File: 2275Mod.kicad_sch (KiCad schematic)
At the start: 22 parts, among them IC1 LTV-356T, J1 640388-8, K1 40.52.8.024.5000, K2 G5LE-14-CF_DC24, U1 LM340LAZ-5.0, U2 TCLT1600, U3 TCLT1600, q1 NPN_Transistor

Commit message: commit before starting kicad 7
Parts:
- C1: footprint (none) -> Capacitor_THT:C_Rect_L10.0mm_W4.0mm_P7.50mm_MKS4
- C2: footprint (none) -> Capacitor_THT:CP_Radial_D16.0mm_P7.50mm
- C3: footprint (none) -> Capacitor_THT:CP_Radial_D5.0mm_P2.50mm
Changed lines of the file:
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@@
       (effects (font (size 1.27 1.27)) (justify left))
     )
-    (property "Footprint" "" (id 2) (at 254.9652 97.79 0)
+    (property "Footprint" "Capacitor_THT:CP_Radial_D5.0mm_P2.50mm" (id 2) (at 254.9652 97.79 0)
       (effects (font (size 1.27 1.27)) hide)
     )
@@
       (effects (font (size 1.27 1.27)) (justify left))
     )
-    (property "Footprint" "" (id 2) (at 77.47 95.25 0)
+    (property "Footprint" "Capacitor_THT:C_Rect_L10.0mm_W4.0mm_P7.50mm_MKS4" (id 2) (at 77.47 95.25 0)
       (effects (font (size 1.27 1.27)) hide)
     )
@@
       (effects (font (size 1.27 1.27)) (justify left))
     )
-    (property "Footprint" "" (id 2) (at 215.5952 96.52 0)
+    (property "Footprint" "Capacitor_THT:CP_Radial_D16.0mm_P7.50mm" (id 2) (at 215.5952 96.52 0)
       (effects (font (size 1.27 1.27)) hide)
     )
@@
     )
     (path "/af6d24d3-2ebe-4f80-9d0c-f289817d2611"
-      (reference "C1") (unit 1) (value ".01/400v") (footprint "")
+      (reference "C1") (unit 1) (value ".01/400v") (footprint "Capacitor_THT:C_Rect_L10.0mm_W4.0mm_P7.50mm_MKS4")
     )
     (path "/f943cf73-6023-4201-8914-d783c8da9ec4"
-      (reference "C2") (unit 1) (value "1000uf") (footprint "")
+      (reference "C2") (unit 1) (value "1000uf") (footprint "Capacitor_THT:CP_Radial_D16.0mm_P7.50mm")
     )
     (path "/281740b4-9504-4250-8402-6cda37c9fff4"
-      (reference "C3") (unit 1) (value "10uf") (footprint "")
+      (reference "C3") (unit 1) (value "10uf") (footprint "Capacitor_THT:CP_Radial_D5.0mm_P2.50mm")
     )
     (path "/9ee275cc-47c1-4b8b-980c-7d7214ee4bde/5b26e194-09b4-48bf-9fc7-24c57264e72b"
@@
     )
     (path "/9ee275cc-47c1-4b8b-980c-7d7214ee4bde/b240069a-d2aa-48dc-9bba-60a372f4e603"
-      (reference "C201") (unit 1) (value "4700uf") (footprint "")
+      (reference "C201") (unit 1) (value "4700uf") (footprint "Capacitor_THT:CP_Radial_D25.0mm_P10.00mm_SnapIn")
     )
     (path "/1c064150-4a5c-4345-8f52-f032fa5cdc84"
@@
     )
     (path "/9ee275cc-47c1-4b8b-980c-7d7214ee4bde/4f791885-332d-4c42-9ab4-d18f400bce56"
-      (reference "R205") (unit 1) (value "220") (footprint "")
+      (reference "R205") (unit 1) (value "220") (footprint "Resistor_SMD:R_0805_2012Metric_Pad1.20x1.40mm_HandSolder")
     )
     (path "/44cf2d32-8e8c-4f2d-a00f-594cc953fa48"

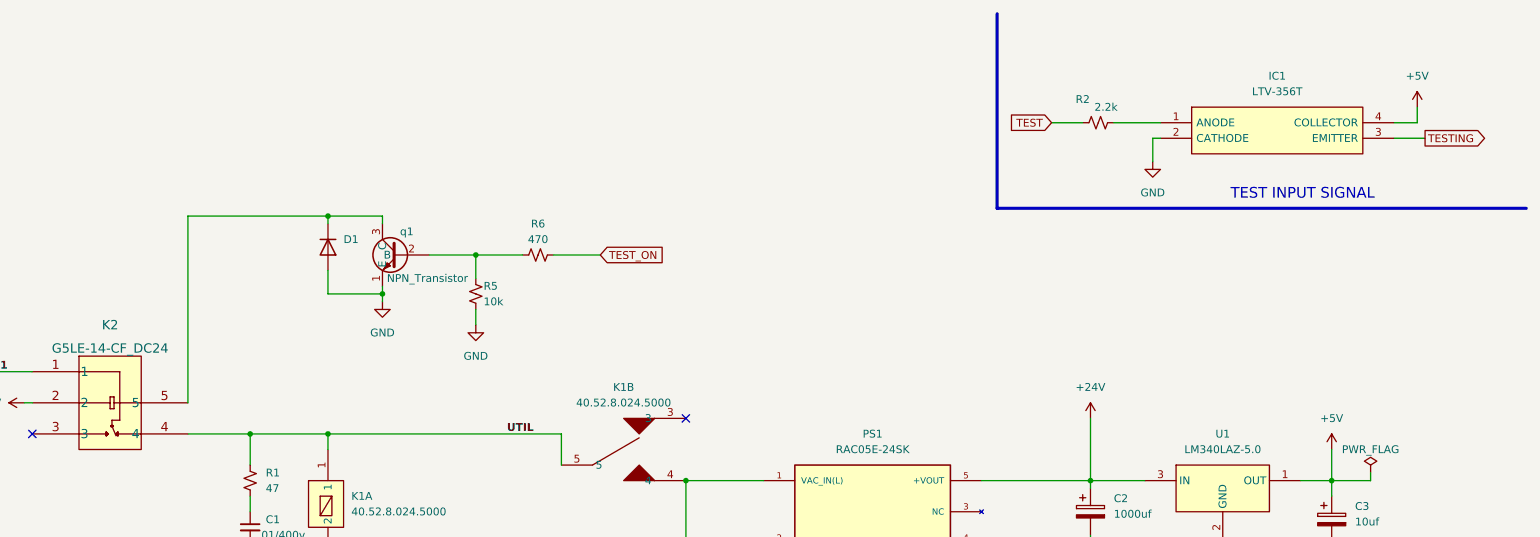
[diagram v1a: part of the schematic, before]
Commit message: move parts on the PCB
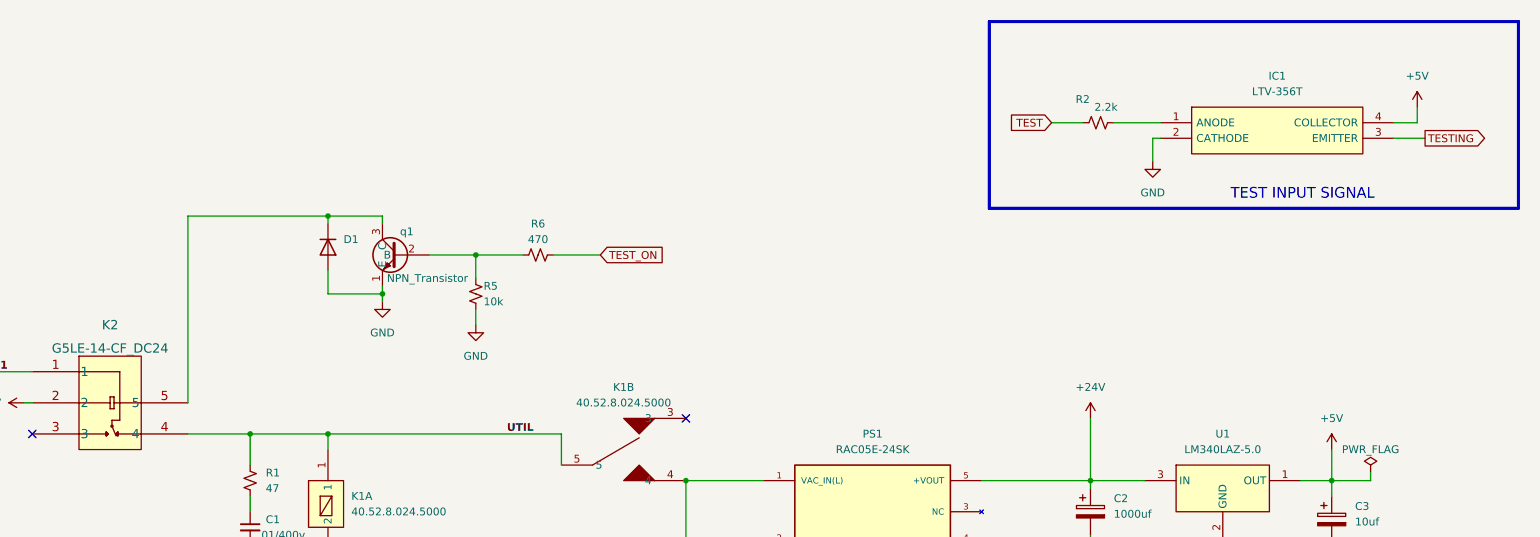
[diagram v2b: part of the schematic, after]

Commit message: add test points, clean up errors
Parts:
- added TP1, TP2, TP3: 5019, AAA_Misc:KEYSTONE_5019, symbol AAA_Misc:5019
- C1: footprint Capacitor_THT:C_Rect_L10.0mm_W4.0mm_P7.50mm_MKS4 -> AAA_Misc:KEYSTONE_5019
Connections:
- net +24V: now also TP1.TP
- net +5V: now also TP2.TP
- net GND: now also TP3.TP
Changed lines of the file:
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@@
   (junction (at 254 87.63) (diameter 0) (color 0 0 0 0)
   )
+  (junction (at 203.2 97.79) (diameter 0) (color 0 0 0 0)
+  )
+  (junction (at 254 78.74) (diameter 0) (color 0 0 0 0)
+  )
   (junction (at 77.47 102.87) (diameter 0) (color 0 0 0 0)
   )
@@
   )
   (junction (at 214.63 97.79) (diameter 0) (color 0 0 0 0)
+  )
+  (junction (at 214.63 80.01) (diameter 0) (color 0 0 0 0)
   )
   (junction (at 77.47 80.01) (diameter 0) (color 0 0 0 0)
@@
     (stroke (width 0) (type default))
   )
+  (wire (pts (xy 214.63 80.01) (xy 214.63 87.63))
+    (stroke (width 0) (type default))
+  )
+  (wire (pts (xy 254 78.74) (xy 256.54 78.74))
+    (stroke (width 0) (type default))
+  )
   (polyline (pts (xy 20.32 166.37) (xy 20.32 196.85))
     (stroke (width 0.5) (type solid) (color 0 0 0 1))
   )
+  (wire (pts (xy 254 78.74) (xy 254 77.47))
+    (stroke (width 0) (type default))
+  )
   (polyline (pts (xy 92.71 166.37) (xy 20.32 166.37))
     (stroke (width 0.5) (type solid) (color 0 0 0 1))
   )
+  (wire (pts (xy 212.09 80.01) (xy 214.63 80.01))
+    (stroke (width 0) (type default))
+  )
   (wire (pts (xy 248.92 87.63) (xy 254 87.63))
     (stroke (width 0) (type default))
@@
     (stroke (width 0) (type default))
   )
-  (wire (pts (xy 254 87.63) (xy 254 82.55))
+  (wire (pts (xy 254 87.63) (xy 254 78.74))
     (stroke (width 0) (type default))
   )
@@
     (stroke (width 0.5) (type solid) (color 0 0 0 1))
   )
+  (wire (pts (xy 203.2 97.79) (xy 214.63 97.79))
+    (stroke (width 0) (type default))
+  )
   (wire (pts (xy 226.06 31.75) (xy 224.79 31.75))
     (stroke (width 0) (type default))
@@
     (stroke (width 0) (type default))
   )
-  (wire (pts (xy 196.85 97.79) (xy 214.63 97.79))
+  (wire (pts (xy 196.85 97.79) (xy 203.2 97.79))
     (stroke (width 0) (type default))
   )
@@
     (stroke (width 0) (type default))
   )
+  (wire (pts (xy 203.2 97.79) (xy 203.2 100.33))
+    (stroke (width 0) (type default))
+  )
   (wire (pts (xy 77.47 102.87) (xy 90.17 102.87))
     (stroke (width 0) (type default))
@@
     (stroke (width 0) (type default))
   )
+  (wire (pts (xy 254 132.08) (xy 260.35 132.08))
+    (stroke (width 0) (type default))
+  )
   (wire (pts (xy 127 50.8) (xy 134.62 50.8))
     (stroke (width 0) (type default))
@@
     (stroke (width 0) (type default))
   )
-  (wire (pts (xy 214.63 77.47) (xy 214.63 87.63))
+  (wire (pts (xy 214.63 77.47) (xy 214.63 80.01))
     (stroke (width 0) (type default))
   )
@@
   (label "G_L1" (at 101.6 176.53 0) (fields_autoplaced)
     (effects (font (size 1.27 1.27) bold) (justify left bottom))
+  )
+  (label "+24V" (at 204.47 87.63 0) (fields_autoplaced)
+    (effects (font (size 1.27 1.27)) (justify left bottom))
+  )
+  (label "5VDC" (at 255.27 87.63 0) (fields_autoplaced)
+    (effects (font (size 1 1)) (justify left bottom))
   )
   (label "L1" (at 35.56 69.85 0) (fields_autoplaced)
@@
         (path "/6ee24427-09ce-46d0-a3a3-2e623f3a3aa5"
           (reference "R5") (unit 1)
+        )
+      )
+    )
+  )
+  (symbol (lib_id "AAA_Misc:5019") (at 207.01 80.01 180) (unit 1)
+    (in_bom yes) (on_board yes) (dnp no) (fields_autoplaced)
+    (property "Reference" "TP1" (at 207.01 74.93 0)
+      (effects (font (size 1.27 1.27)))
+    )
+    (property "Value" "5019" (at 207.01 77.47 0)
+      (effects (font (size 1.27 1.27)))
+    )
+    (property "Footprint" "AAA_Misc:KEYSTONE_5019" (at 203.2 76.2 0)
+      (effects (font (size 1.27 1.27)) (justify left bottom) hide)
+    )
+    (property "Datasheet" "" (at 207.01 80.01 0)
+      (effects (font (size 1.27 1.27)) (justify left bottom) hide)
+    )
+    (property "PARTREV" "D" (at 207.01 80.01 0)
+      (effects (font (size 1.27 1.27)) (justify left bottom) hide)
+    )
+    (property "STANDARD" "Manufacturer Recommendations" (at 205.74 82.55 0)
+      (effects (font (size 1.27 1.27)) (justify left bottom) hide)
+    )
+    (property "MAXIMUM_PACKAGE_HEIGHT" "2.29 mm" (at 201.93 80.01 0)
+      (effects (font (size 1.27 1.27)) (justify left bottom) hide)
+    )
+    (property "MANUFACTURER" "Keystone Electronics" (at 205.74 83.82 0)
+      (effects (font (size 1.27 1.27)) (justify left bottom) hide)
+    )
+    (property "SNAPEDA_PN" "5019" (at 214.63 74.93 0)
+      (effects (font (size 1.27 1.27)) (justify left bottom) hide)
+    )
+    (pin "TP")
+    (instances
+      (project "2275Mod"
+        (path "/6ee24427-09ce-46d0-a3a3-2e623f3a3aa5"
+          (reference "TP1") (unit 1)
         )
       )
@@
     )
   )
+  (symbol (lib_id "AAA_Misc:5019") (at 261.62 78.74 0) (unit 1)
+    (in_bom yes) (on_board yes) (dnp no) (fields_autoplaced)
+    (property "Reference" "TP2" (at 264.16 78.105 0)
+      (effects (font (size 1.27 1.27)) (justify left))
+    )
+    (property "Value" "5019" (at 264.16 80.645 0)
+      (effects (font (size 1.27 1.27)) (justify left))
+    )
+    (property "Footprint" "AAA_Misc:KEYSTONE_5019" (at 265.43 82.55 0)
+      (effects (font (size 1.27 1.27)) (justify left bottom) hide)
+    )
+    (property "Datasheet" "" (at 261.62 78.74 0)
+      (effects (font (size 1.27 1.27)) (justify left bottom) hide)
+    )
+    (property "PARTREV" "D" (at 261.62 78.74 0)
+      (effects (font (size 1.27 1.27)) (justify left bottom) hide)
+    )
+    (property "STANDARD" "Manufacturer Recommendations" (at 262.89 76.2 0)
+      (effects (font (size 1.27 1.27)) (justify left bottom) hide)
+    )
+    (property "MAXIMUM_PACKAGE_HEIGHT" "2.29 mm" (at 266.7 78.74 0)
+      (effects (font (size 1.27 1.27)) (justify left bottom) hide)
+    )
+    (property "MANUFACTURER" "Keystone Electronics" (at 262.89 74.93 0)
+      (effects (font (size 1.27 1.27)) (justify left bottom) hide)
+    )
+    (property "SNAPEDA_PN" "5019" (at 254 83.82 0)
+      (effects (font (size 1.27 1.27)) (justify left bottom) hide)
+    )
+    (pin "TP")
+    (instances
+      (project "2275Mod"
+        (path "/6ee24427-09ce-46d0-a3a3-2e623f3a3aa5"
+          (reference "TP2") (unit 1)
+        )
+      )
+    )
+  )
   (symbol (lib_id "Device:R_Small_US") (at 215.9 29.21 90) (unit 1)
     (in_bom yes) (on_board yes) (dnp no)
@@
     )
   )
+  (symbol (lib_id "AAA_Misc:5019") (at 203.2 105.41 270) (unit 1)
+    (in_bom yes) (on_board yes) (dnp no) (fields_autoplaced)
+    (property "Reference" "TP3" (at 205.74 104.775 90)
+      (effects (font (size 1.27 1.27)) (justify left))
+    )
+    (property "Value" "5019" (at 205.74 107.315 90)
+      (effects (font (size 1.27 1.27)) (justify left))
+    )
+    (property "Footprint" "AAA_Misc:KEYSTONE_5019" (at 199.39 109.22 0)
+      (effects (font (size 1.27 1.27)) (justify left bottom) hide)
+    )
+    (property "Datasheet" "" (at 203.2 105.41 0)
+      (effects (font (size 1.27 1.27)) (justify left bottom) hide)
+    )
+    (property "PARTREV" "D" (at 203.2 105.41 0)
+      (effects (font (size 1.27 1.27)) (justify left bottom) hide)
+    )
+    (property "STANDARD" "Manufacturer Recommendations" (at 205.74 106.68 0)
+      (effects (font (size 1.27 1.27)) (justify left bottom) hide)
+    )
+    (property "MAXIMUM_PACKAGE_HEIGHT" "2.29 mm" (at 203.2 110.49 0)
+      (effects (font (size 1.27 1.27)) (justify left bottom) hide)
+    )
+    (property "MANUFACTURER" "Keystone Electronics" (at 207.01 106.68 0)
+      (effects (font (size 1.27 1.27)) (justify left bottom) hide)
+    )
+    (property "SNAPEDA_PN" "5019" (at 198.12 97.79 0)
+      (effects (font (size 1.27 1.27)) (justify left bottom) hide)
+    )
+    (pin "TP")
+    (instances
+      (project "2275Mod"
+        (path "/6ee24427-09ce-46d0-a3a3-2e623f3a3aa5"
+          (reference "TP3") (unit 1)
+        )
+      )
+    )
+  )
   (symbol (lib_id "AAA_JH:LTV-356T") (at 226.06 29.21 0) (unit 1)
     (in_bom yes) (on_board yes) (dnp no) (fields_autoplaced)
@@
     )
   )
-  (symbol (lib_id "power:+5V") (at 254 82.55 0) (unit 1)
-    (in_bom yes) (on_board yes) (dnp no) (fields_autoplaced)
-    (property "Reference" "#PWR08" (at 254 86.36 0)
-      (effects (font (size 1.27 1.27)) hide)
-    )
-    (property "Value" "+5V" (at 254 77.47 0)
-      (effects (font (size 1.27 1.27)))
-    )
-    (property "Footprint" "" (at 254 82.55 0)
-      (effects (font (size 1.27 1.27)) hide)
-    )
-    (property "Datasheet" "" (at 254 82.55 0)
+  (symbol (lib_id "power:+5V") (at 254 77.47 0) (unit 1)
+    (in_bom yes) (on_board yes) (dnp no) (fields_autoplaced)
+    (property "Reference" "#PWR08" (at 254 81.28 0)
+      (effects (font (size 1.27 1.27)) hide)
+    )
+    (property "Value" "+5V" (at 254 72.39 0)
+      (effects (font (size 1.27 1.27)))
+    )
+    (property "Footprint" "" (at 254 77.47 0)
+      (effects (font (size 1.27 1.27)) hide)
+    )
+    (property "Datasheet" "" (at 254 77.47 0)
       (effects (font (size 1.27 1.27)) hide)
     )
@@
       (effects (font (size 1.27 1.27)) (justify left))
     )
-    (property "Footprint" "Capacitor_THT:C_Rect_L10.0mm_W4.0mm_P7.50mm_MKS4" (at 77.47 95.25 0)
+    (property "Footprint" "AAA_Misc:KEYSTONE_5019" (at 77.47 95.25 0)
       (effects (font (size 1.27 1.27)) hide)
     )
@@
       (effects (font (size 1.27 1.27)) hide)
     )
-    (property "Value" "PWR_FLAG" (at 260.35 82.55 0)
-      (effects (font (size 1.27 1.27)))
-    )
+    (property "Value" "PWR_FLAG" (at 266.7 85.09 0)
+      (effects (font (size 1.27 1.27)))
+    )

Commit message: make some traces thicker
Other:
- note added: "Test Relay"
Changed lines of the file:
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@@
     (effects (font (size 1.75 1.75)) (justify left bottom))
+  )
+  (text "Test Relay" (at 49.53 86.36 0)
+    (effects (font (size 1.8 1.8) (thickness 0.254) bold (color 0 0 0 1)) (justify left bottom))
   )
   (text "GENERATOR MONITOR" (at 120.65 195.58 0)

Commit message: corrected q200 and q201 footprints
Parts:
- C1: footprint AAA_Misc:KEYSTONE_5019 -> Capacitor_THT:C_Rect_L9.0mm_W3.8mm_P7.50mm_MKT
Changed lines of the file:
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@@
-    (stroke (width 0) (type default))
-  )
-  (wire (pts (xy 254 132.08) (xy 260.35 132.08))
     (stroke (width 0) (type default))
   )
@@
       (effects (font (size 1.27 1.27)) (justify left))
     )
-    (property "Footprint" "AAA_Misc:KEYSTONE_5019" (at 77.47 95.25 0)
-      (effects (font (size 1.27 1.27)) hide)
-    )
+    (property "Footprint" "Capacitor_THT:C_Rect_L9.0mm_W3.8mm_P7.50mm_MKT" (at 77.47 95.25 0)
+      (effects (font (size 1.27 1.27)) hide)
+    )

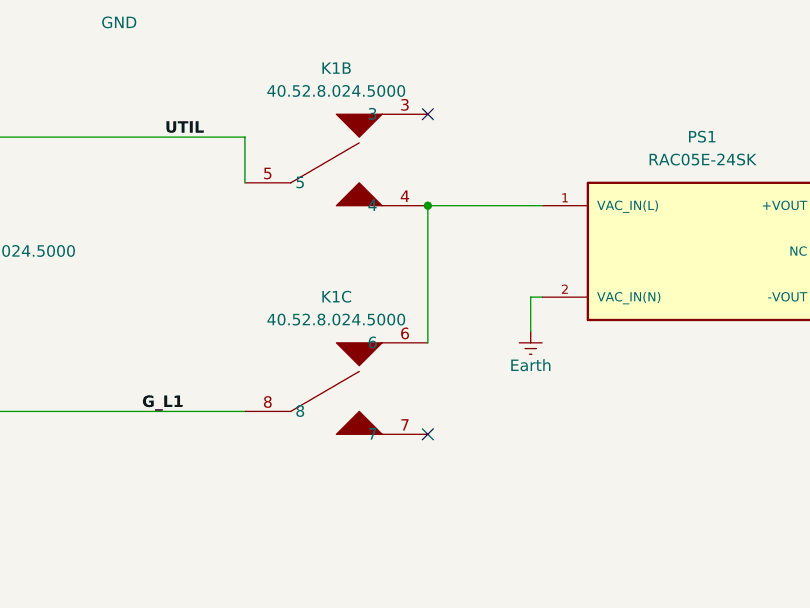
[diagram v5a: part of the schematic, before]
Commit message: fix k1 wrong foot print re route
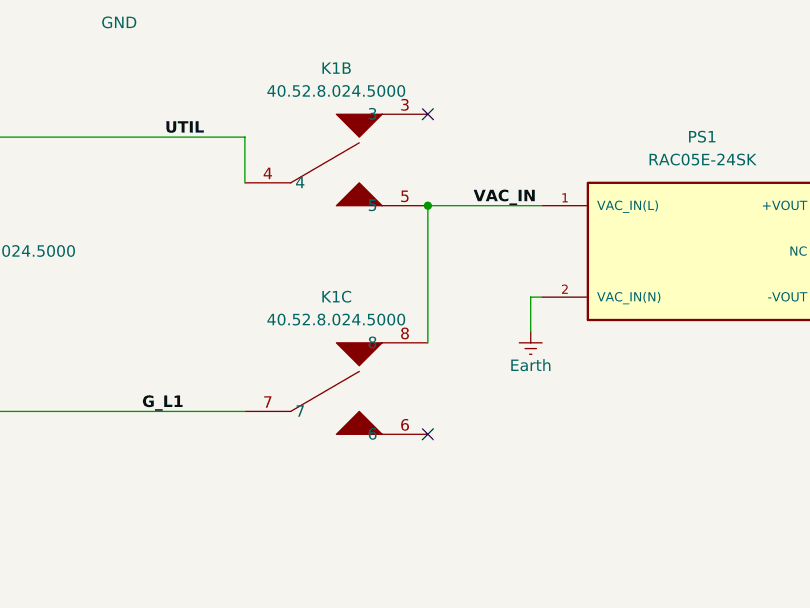
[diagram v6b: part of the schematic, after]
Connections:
- net G_L1: now also K1.7; no longer K1.8
- net UTIL: now also K1.4; no longer K1.5
- new net VAC_IN: K1.5, K1.8, PS1.1 (VAC_IN(L))
- now unconnected: K1.6
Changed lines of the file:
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@@
+    (effects (font (size 1.27 1.27) (thickness 0.254) bold) (justify left bottom))
+  )
+  (label "VAC_IN" (at 153.67 87.63 0) (fields_autoplaced)
     (effects (font (size 1.27 1.27) (thickness 0.254) bold) (justify left bottom))
   )
@@
     )
   )
-  (symbol (lib_id "AAA_JH:40.52.8.024.5000") (at 148.59 97.79 0) (mirror y) (unit 3)
+  (symbol (lib_name "40.52.8.024.5000_2") (lib_id "AAA_JH:40.52.8.024.5000") (at 148.59 97.79 0) (mirror y) (unit 3)
     (in_bom yes) (on_board yes) (dnp no) (fields_autoplaced)
     (property "Reference" "K1" (at 138.43 97.79 0)
@@
     )
   )
-  (symbol (lib_id "AAA_JH:40.52.8.024.5000") (at 91.44 87.63 0) (unit 1)
+  (symbol (lib_name "40.52.8.024.5000_1") (lib_id "AAA_JH:40.52.8.024.5000") (at 91.44 87.63 0) (unit 1)
     (in_bom yes) (on_board yes) (dnp no) (fields_autoplaced)
     (property "Reference" "K1" (at 93.98 90.1699 0)
